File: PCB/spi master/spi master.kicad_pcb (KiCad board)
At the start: 2 copper layers, 76.2 x 43.2 mm, 13 parts, among them J1 n8 Bus Connector, U1 74LS08, U10 74HC273, U11 74HC245, U2 74LS393, U3 74HC04, U4 74LS139, U5 74HC595, U6 74HC165, U8 74HC74, U9 74LS153

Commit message: Final changes for v2
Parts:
- moved U6 11.1 mm to (131.3, 108.8)
- moved U5 11.1 mm to (131.3, 97.9)
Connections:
- net R~W renamed R~{W}
- net ~CS renamed ~{CS}
- net ~CS0 renamed ~{CS0}
- net ~CS1 renamed ~{CS1}
- net ~CS2 renamed ~{CS2}
- net ~CS3 renamed ~{CS3}
- net ~DATA_RD renamed ~{DATA_RD}
- net ~DATA_WR renamed ~{DATA_WR}
- net ~IRQ renamed ~{IRQ}
- net ~RES renamed ~{RES}
- net ~SR_RD renamed ~{SR_RD}
- net ~SR_WR renamed ~{SR_WR}
- net ~TX_COMPLETE renamed ~{TX_COMPLETE}
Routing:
- net SPI_CLK: track 0.00 -> 23.9 mm
- net /D0: track 0.00 -> 17.2 mm
- net /D1: track 0.00 -> 12.9 mm
- net +5V: track 0.00 -> 12.0 mm
- net /D6: track 0.00 -> 12.0 mm
- net D7: track 0.00 -> 12.0 mm
- net /D5: track 0.00 -> 12.0 mm
- net /D4: track 0.00 -> 12.0 mm
- net /D2: track 0.00 -> 6.47 mm
- net /D3: track 0.00 -> 3.35 mm
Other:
- net class Default removed

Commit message: Working simulation...
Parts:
- added U2: 74HC00, Package_DIP:DIP-14_W7.62mm, F.Cu at (123.9, 86.3)
- added U5: 74LS08, Package_DIP:DIP-14_W7.62mm, F.Cu at (126.0, 71.4)
- J1: renamed from e; footprint Connector_PinHeader_2.54mm:PinHeader_1x09_P2.54mm_Horizontal -> Connector_PinSocket_2.54mm:PinSocket_1x09_P2.54mm_Horizontal
- U1: value 74LS08 -> 74LS393
- moved U9 62.3 mm to (103.9, 86.3), turned to 90 degrees
- moved J1 38.4 mm to (166.4, 67.6), turned to 180 degrees
- moved U1 34.2 mm to (146.0, 71.4), turned to 90 degrees
- moved U3 28.6 mm to (121.7, 63.8), turned to -90 degrees
- moved U8 21.7 mm to (167.1, 93.0), turned to 0 degrees
- moved U4 17.6 mm to (144.0, 86.3)
- moved U6 0.14 mm to (131.2, 97.7)
- moved U7 0.14 mm to (131.2, 108.7)
- renumbered J1 to J2, U9 to U10, U10 to U11, U11 to U12, U4 to U3, U3 to U4, U5 to U6, U6 to U7, U2 to U8, U8 to U9
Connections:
- net ~{SR_RD} renamed ~{CR_RD}
- J1 pad 8: ~{CS3} -> ~{CS2}
- J2 pad 18: Net-(J1-Pad18) -> unconnected-(J2-Pin_18-Pad18)
- J2 pad 20: Net-(J1-Pad20) -> unconnected-(J2-Pin_20-Pad20)
- J2 pad 22: Net-(J1-Pad22) -> unconnected-(J2-Pin_22-Pad22)
- J2 pad 24: Net-(J1-Pad24) -> unconnected-(J2-Pin_24-Pad24)
- J2 pad 26: Net-(J1-Pad26) -> unconnected-(J2-Pin_26-Pad26)
- J2 pad 5: Net-(J1-Pad5) -> unconnected-(J2-Pin_5-Pad5)
- J2 pad 6: Net-(J1-Pad6) -> unconnected-(J2-Pin_6-Pad6)
- J2 pad 7: Net-(J1-Pad7) -> unconnected-(J2-Pin_7-Pad7)
- J2 pad 8: Net-(J1-Pad8) -> unconnected-(J2-Pin_8-Pad8)
- J2 pad 9: Net-(J1-Pad9) -> unconnected-(J2-Pin_9-Pad9)
- U1 pad 1: Net-(U1-Pad1) -> ~{DIV_CLK}
- U1 pad 10: DIV_CLK -> unconnected-(U1B-Q1-Pad10)
- U1 pad 11: Net-(U1-Pad11) -> TX_COMPLETE
- U1 pad 12: ITC -> Net-(U1A-MR)
- U1 pad 13: IEN -> Net-(U1A-Q3)
- U1 pad 14: +5V -> unconnected-(U1C-VCC-Pad14)
- U1 pad 2: ~{RES} -> Net-(U1A-MR)
- U1 pad 3: ~{TX_COMPLETE} -> SPI_CLK
- U1 pad 4: (no net) -> unconnected-(U1A-Q1-Pad4)
- U1 pad 5: (no net) -> unconnected-(U1A-Q2-Pad5)
- U1 pad 6: (no net) -> Net-(U1A-Q3)
- U1 pad 7: GND -> +5V
- U1 pad 8: SPI_CLK -> unconnected-(U1B-Q3-Pad8)
- U1 pad 9: RUNNING -> unconnected-(U1B-Q2-Pad9)
- U10 pad 6: Net-(U2-Pad3) -> CLK
- U10 pad 9: Net-(U9-Pad9) -> unconnected-(U10-Zb-Pad9)
- U11 pad 11: ~{SR_WR} -> ~{CR_WR}_{QUAL}
- U11 pad 19: Net-(U10-Pad19) -> unconnected-(U11-Q7-Pad19)
- U3 pad 10: ~{SR_WR} -> ~{CR_WR}
- U3 pad 7: ~{CS3} -> ~{CS2}
- U4 pad 1: ~{TX_COMPLETE} -> Net-(U7-Q7)
- U4 pad 10: (no net) -> Net-(U2-Pad10)
- U4 pad 11: (no net) -> ~{DATA_WR}
- U4 pad 12: (no net) -> ~{SPI_CLK}
- U4 pad 13: (no net) -> SPI_CLK
- U4 pad 2: TX_COMPLETE -> Net-(U2-Pad4)
- U4 pad 3: Net-(U2-Pad9) -> TX_COMPLETE
- U4 pad 4: Net-(U1-Pad1) -> Net-(U4-Pad4)
- U4 pad 8: ~{IRQ} -> Net-(U4-Pad8)
- U4 pad 9: Net-(U1-Pad11) -> ~{CR_WR}
- U6 pad 9: Net-(U5-Pad9) -> unconnected-(U6-QH'-Pad9)
- U7 pad 1: ~{DATA_WR} -> ~{DATA_WR}_{QUAL}
- U7 pad 10: +5V -> VCC
- U7 pad 2: SPI_CLK -> ~{SPI_CLK}
- U7 pad 7: Net-(U6-Pad7) -> unconnected-(U7-~{Q7}-Pad7)
- U7 pad 9: MOSI -> Net-(U7-Q7)
- U8 pad 10: Net-(U2-Pad10) -> unconnected-(U8B-Q1-Pad10)
- U8 pad 11: Net-(U2-Pad11) -> unconnected-(U8B-Q0-Pad11)
- U8 pad 12: TX_COMPLETE -> GND
- U8 pad 13: SPI_CLK -> VCC
- U8 pad 2: ~{RES} -> GND
- U8 pad 3: Net-(U2-Pad3) -> unconnected-(U8A-Q0-Pad3)
- U8 pad 8: Net-(U2-Pad8) -> unconnected-(U8B-Q3-Pad8)
- U8 pad 9: Net-(U2-Pad9) -> unconnected-(U8B-Q2-Pad9)
- U9 pad 1: ~{RES} -> ~{ITC_RES}
- U9 pad 11: Net-(U8-Pad11) -> unconnected-(U9B-C-Pad11)
- U9 pad 12: Net-(U8-Pad12) -> unconnected-(U9B-D-Pad12)
- U9 pad 13: ~{TX_COMPLETE} -> ~{TX_COMPLETE_RES}
- U9 pad 3: ~{SR_WR} -> ~{CR_WR}
- U9 pad 6: Net-(U8-Pad6) -> unconnected-(U9A-~{Q}-Pad6)
- U9 pad 8: Net-(U8-Pad8) -> unconnected-(U9B-~{Q}-Pad8)

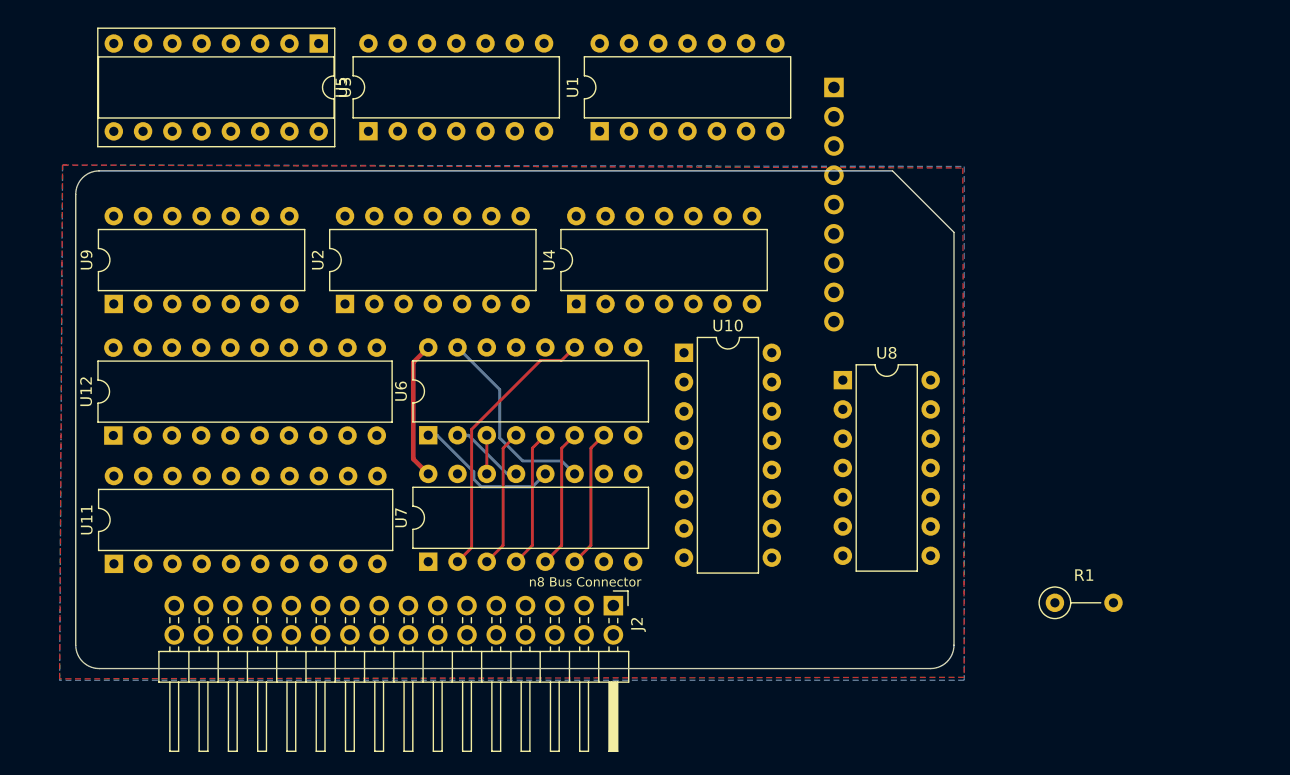
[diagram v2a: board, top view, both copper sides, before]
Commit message: 3 signals away from SPI Master PCB
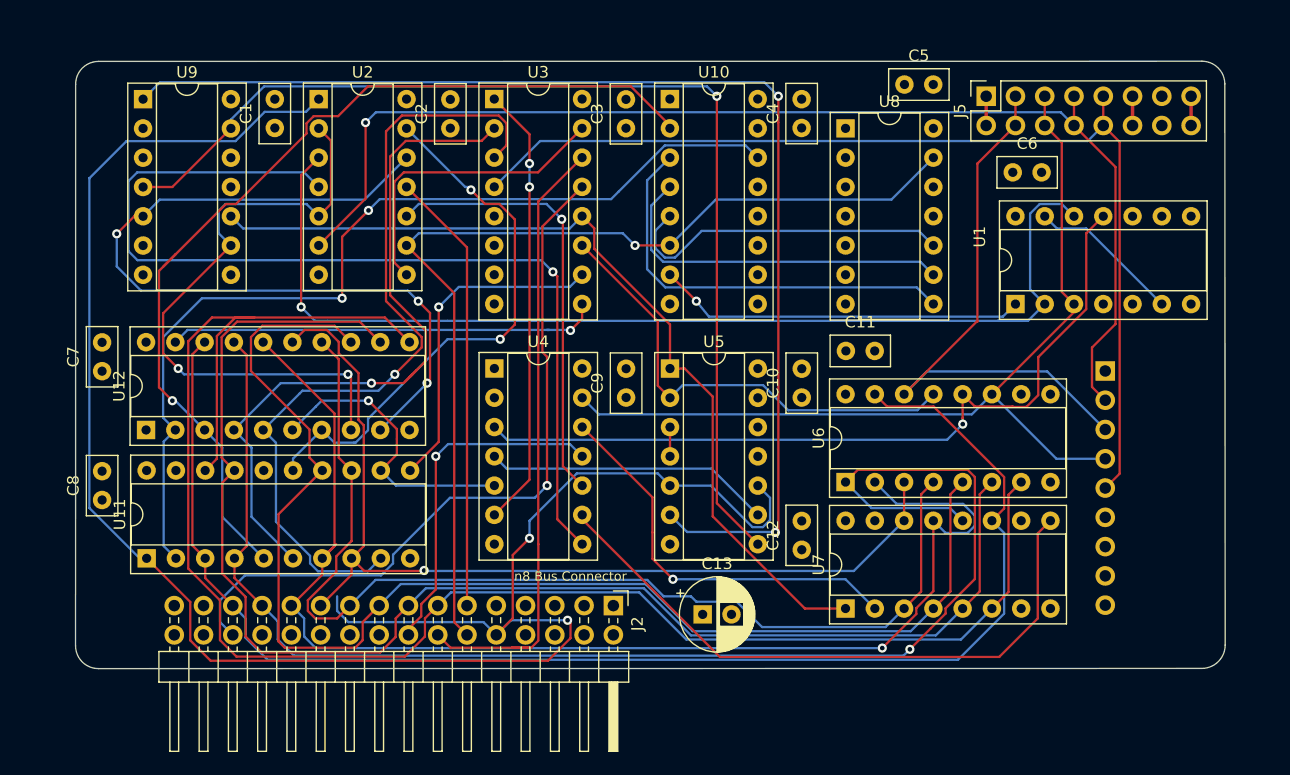
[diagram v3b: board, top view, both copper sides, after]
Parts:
- removed R1: 20K, Resistor_THT:R_Axial_DIN0207_L6.3mm_D2.5mm_P5.08mm_Vertical
- added C1: 100nf, Capacitor_THT:C_Disc_D5.0mm_W2.5mm_P2.50mm, F.Cu at (117.9, 71.1)
- added C10: 100nf, Capacitor_THT:C_Disc_D5.0mm_W2.5mm_P2.50mm, F.Cu at (163.6, 94.5)
- added C11: 100nf, Capacitor_THT:C_Disc_D5.0mm_W2.5mm_P2.50mm, F.Cu at (167.4, 90.4)
- added C12: 100nf, Capacitor_THT:C_Disc_D5.0mm_W2.5mm_P2.50mm, F.Cu at (163.6, 107.7)
- added C13: 220uf, Capacitor_THT:CP_Radial_D6.3mm_P2.50mm, F.Cu at (155.0, 113.3)
- added C2: 100nf, Capacitor_THT:C_Disc_D5.0mm_W2.5mm_P2.50mm, F.Cu at (133.1, 71.1)
- added C3: 100nf, Capacitor_THT:C_Disc_D5.0mm_W2.5mm_P2.50mm, F.Cu at (148.3, 71.1)
- added C4: 100nf, Capacitor_THT:C_Disc_D5.0mm_W2.5mm_P2.50mm, F.Cu at (163.6, 71.1)
- added C5: 100nf, Capacitor_THT:C_Disc_D5.0mm_W2.5mm_P2.50mm, F.Cu at (172.5, 67.3)
- added C6: 100nf, Capacitor_THT:C_Disc_D5.0mm_W2.5mm_P2.50mm, F.Cu at (181.9, 74.9)
- added C7: 100nf, Capacitor_THT:C_Disc_D5.0mm_W2.5mm_P2.50mm, F.Cu at (102.9, 92.2)
- added C8: 100nf, Capacitor_THT:C_Disc_D5.0mm_W2.5mm_P2.50mm, F.Cu at (102.9, 103.4)
- added C9: 100nf, Capacitor_THT:C_Disc_D5.0mm_W2.5mm_P2.50mm, F.Cu at (148.3, 94.5)
- added J5: SD_CARD_PORT, Connector_PinSocket_2.54mm:PinSocket_2x08_P2.54mm_Vertical, F.Cu at (179.6, 68.3)
- U1, U2, U4, U5, U8, U9: footprint Package_DIP:DIP-14_W7.62mm -> Package_DIP:DIP-14_W7.62mm_Socket
- U10, U6, U7: footprint Package_DIP:DIP-16_W7.62mm -> Package_DIP:DIP-16_W7.62mm_Socket
- U11, U12: footprint Package_DIP:DIP-20_W7.62mm -> Package_DIP:DIP-20_W7.62mm_Socket
- moved U1 39.1 mm to (182.1, 86.4)
- moved U6 36.4 mm to (167.4, 101.8)
- moved U7 36.4 mm to (167.4, 112.8)
- moved J1 34.0 mm to (189.9, 92.2)
- moved U5 33.3 mm to (152.1, 92.0), turned to 0 degrees
- moved U10 22.1 mm to (152.1, 68.6)
- moved U8 21.8 mm to (167.4, 71.1)
- moved U9 18.0 mm to (106.4, 68.6), turned to 0 degrees
- moved U2 17.9 mm to (121.7, 68.6), turned to 0 degrees
- moved U3 16.0 mm to (136.9, 68.6), turned to 0 degrees
- moved U4 9.05 mm to (136.9, 91.9), turned to 0 degrees
- moved U12 2.88 mm to (106.7, 97.3)
- moved U11 2.88 mm to (106.7, 108.4)
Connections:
- net ~{CR_RD} renamed ~{CTRL_RD}
- J1 pad 8: ~{CS2} -> ~{CS3}
- J2 pad 13: D7 -> /D7
- U1 pad 1: ~{DIV_CLK} -> DIV_CLK
- U1 pad 14: unconnected-(U1C-VCC-Pad14) -> +5V
- U1 pad 7: +5V -> GND
- U11 pad 11: ~{CR_WR}_{QUAL} -> ~{CTRL_WR}
- U11 pad 16: /UNUSED -> unconnected-(U11-Q6-Pad16)
- U11 pad 18: D7 -> /D7
- U12 pad 11: D7 -> /D7
- U12 pad 8: /UNUSED -> RUNNING
- U2 pad 14: unconnected-(U2E-VCC-Pad14) -> +5V
- U2 pad 7: unconnected-(U2E-GND-Pad7) -> GND
- U2 pad 8: ~{DATA_WR}_{QUAL} -> ~{CS}_{QUAL}
- U3 pad 10: ~{CR_WR} -> ~{CTRL_WR}
- U3 pad 13: R~{W} -> A0
- U3 pad 14: A0 -> R~{W}
- U3 pad 15: ~{CS} -> ~{CS}_{QUAL}
- U3 pad 7: ~{CS2} -> ~{CS3}
- U4 pad 1: Net-(U7-Q7) -> GND
- U4 pad 11: ~{DATA_WR} -> ~{CS}
- U4 pad 2: Net-(U2-Pad4) -> unconnected-(U4-Pad2)
- U4 pad 8: Net-(U4-Pad8) -> Net-(U2-Pad4)
- U4 pad 9: ~{CR_WR} -> Net-(U7-Q7)
- U5 pad 11: ~{CR_WR}_{QUAL} -> unconnected-(U5-Pad11)
- U5 pad 12: Net-(U4-Pad8) -> +5V
- U5 pad 13: CLK -> +5V
- U6 pad 10: ~{RES} -> +5V
- U6 pad 7: D7 -> /D7
- U7 pad 1: ~{DATA_WR}_{QUAL} -> ~{DATA_WR}
- U7 pad 10: VCC -> +5V
- U7 pad 6: D7 -> /D7
- U8 pad 1: CLK -> +5V
- U8 pad 10: unconnected-(U8B-Q1-Pad10) -> Net-(U10-I1a)
- U8 pad 13: VCC -> CLK
- U8 pad 4: Net-(U10-I1a) -> unconnected-(U8A-Q1-Pad4)
- U8 pad 5: Net-(U10-I2a) -> unconnected-(U8A-Q2-Pad5)
- U8 pad 6: Net-(U10-I3a) -> unconnected-(U8A-Q3-Pad6)
- U8 pad 8: unconnected-(U8B-Q3-Pad8) -> Net-(U10-I3a)
- U8 pad 9: unconnected-(U8B-Q2-Pad9) -> Net-(U10-I2a)
- U9 pad 11: unconnected-(U9B-C-Pad11) -> +5V
- U9 pad 12: unconnected-(U9B-D-Pad12) -> +5V
- U9 pad 2: D7 -> +5V
- U9 pad 3: ~{CR_WR} -> +5V
- U9 pad 4: ~{TX_COMPLETE} -> ~{TX_COMPLETE_RES}
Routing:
- net ~{RES}: track 0.00 -> 164.9 mm, vias 0 -> 2
- net /D7: track 0.00 -> 149.6 mm
- net /D1: track 12.9 -> 124.7 mm, vias 0 -> 1
- net /D6: track 12.0 -> 123.5 mm
- net /D0: track 17.2 -> 123.2 mm
- net ~{ITC_RES}: track 0.00 -> 104.0 mm, vias 0 -> 2
- net /D2: track 6.47 -> 110.4 mm, vias 0 -> 1
- net MOSI: track 0.00 -> 103.8 mm, vias 0 -> 1
- net /D5: track 12.0 -> 115.0 mm
- net Net-(U1A-MR): track 0.00 -> 94.6 mm, vias 0 -> 1
- net ~{TX_COMPLETE_RES}: track 0.00 -> 94.5 mm, vias 0 -> 1
- net ~{CS0}: track 0.00 -> 90.1 mm
- net CLK: track 0.00 -> 85.7 mm, vias 0 -> 1
- net Net-(U2-Pad4): track 0.00 -> 85.7 mm, vias 0 -> 1
- net DIV1: track 0.00 -> 83.5 mm, vias 0 -> 1
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- added copper zone on In2.Cu, net +5V
- added copper zone on In1.Cu, net GND
- removed copper zone on B.Cu, net (none)
- removed copper zone on F.Cu, net (none)
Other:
- board size 76.2 x 43.2 mm -> 99.7 x 52.7 mm
- copper layers 2 -> 4

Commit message: rc1 for SPI Gate (prev SPI master) rc1 for Bouncer
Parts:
- added D1: LED, LED_SMD:LED_0805_2012Metric_Pad1.15x1.40mm_HandSolder, F.Cu at (197.1, 115.8)
- added R1: 330R, Resistor_SMD:R_0805_2012Metric_Pad1.20x1.40mm_HandSolder, F.Cu at (190.5, 115.8)
- moved C11 0.25 mm to (167.4, 90.2)
- moved C6 0.25 mm to (181.9, 74.7)
- moved C7 0.25 mm to (102.6, 92.2)
- moved C8 0.25 mm to (102.6, 103.4)
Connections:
- U9 pad 8: unconnected-(U9B-~{Q}-Pad8) -> Net-(D1-K)
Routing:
- net Net-(D1-K): track 0.00 -> 144.2 mm, vias 0 -> 1
- net ~{CS2}: track 0.00 -> 76.7 mm
- net ~{CS3}: track 0.00 -> 75.3 mm
- net ~{CS1}: track 0.00 -> 70.1 mm
- net ~{RES}: track 164.9 -> 147.1 mm
- net +5V: track 2.54 -> 19.6 mm
- net Net-(D1-A): track 0.00 -> 4.57 mm
- net Net-(U1A-MR): track 94.6 -> 92.2 mm
- net SEL0: track 63.3 -> 61.5 mm
- net Net-(U2-Pad4): track 85.7 -> 87.5 mm
- net DIV1: track 83.5 -> 81.7 mm
- net R~{W}: track 54.5 -> 52.9 mm
- net ~{CS}: track 30.1 -> 29.5 mm
- net ~{CS}_{QUAL}: track 26.7 -> 27.1 mm, vias 0 -> 1
- net Net-(U3A-E): vias 2 -> 0
- added copper zone on B.Cu, net GND
- added copper zone on F.Cu, net GND
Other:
- board text added: "+5V"
- board text added: "Busy"
- board text added: "Clock"
- board text added: "Control Register"
- board text added: "Data Register"
- board text added: "GND"
- board text added: "MISO"
- board text added: "MOSI"
- board text added: "SCK"
- board text added: "SPI Gate"
- board text added: "State Machine"
- board text added: "by Nate Rivard https://github.com/nrivard/n8-bit Version 1 Nov 2024"
- board text added: "~{CS0}"
- board text added: "~{CS1}"
- board text added: "~{CS2}"
- board text added: "~{CS3}"
- board text removed: "by Nate Rivard https://github.com/nrivard/lmaos Version 1 Mar 2021"

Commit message: Added SpiMaster support
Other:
- board text added: "JLCJLCJLCJLC"
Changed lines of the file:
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@@
 			(outputformat 1)
 			(mirror no)
-			(drillshape 1)
+			(drillshape 0)
 			(scaleselection 1)
-			(outputdirectory "")
+			(outputdirectory "gerbers/")
 		)
 	)
@@
 		(layer "Edge.Cuts")
 	)
+	(gr_line
+		(start 102.550759 117.986977)
+		(end 198.283359 117.972559)
+		(stroke
+			(width 0.05)
+			(type default)
+		)
+		(layer "Edge.Cuts")
+	)
 	(gr_arc
 		(start 200.315359 115.940559)
@@
 		)
 	)
+	(gr_text "JLCJLCJLCJLC"
+		(at 199.4408 98.512 90)
+		(layer "B.SilkS")
+		(effects
+			(font
+				(size 1 1)
+				(thickness 0.15)
+			)
+			(justify left bottom mirror)
+		)
+	)
